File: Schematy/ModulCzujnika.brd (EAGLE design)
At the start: 22.8 x 44.1 mm, 10 parts, among them X1 GLX-S-88M

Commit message: Dodanie podciągającego rezystora na wyjście lm393
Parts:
- added R1: 10k, rcl:0207/7
- R12: value 100k -> 10k
- R13: value 1k -> 5k
- R14: value 1k -> 10k
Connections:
- net N$24: now also R1.2
- net VCC: now also R1.1
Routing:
- net N$24: track 22.5 -> 26.8 mm
- net VCC: track 42.9 -> 47.0 mm
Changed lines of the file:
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@@
 <attribute name="VALUE" x="0.1016" y="27.0256" size="1.27" layer="27" ratio="10" rot="R270"/>
 </element>
-<element name="R12" library="pot" library_urn="urn:adsk.eagle:library:331" package="CA6V" package3d_urn="urn:adsk.eagle:package:22691/1" value="100k" x="13.97" y="7.62" smashed="yes" rot="R90">
-<attribute name="NAME" x="9.779" y="5.08" size="1.27" layer="25" ratio="10" rot="R90"/>
+<element name="R12" library="pot" library_urn="urn:adsk.eagle:library:331" package="CA6V" package3d_urn="urn:adsk.eagle:package:22691/1" value="10k" x="13.97" y="7.62" smashed="yes" rot="R90">
+<attribute name="NAME" x="13.589" y="11.049" size="1.27" layer="25" ratio="10" rot="R180"/>
 <attribute name="POPULARITY" value="10" x="36.83" y="25.4" size="1.778" layer="27" rot="R90" display="off"/>
-<attribute name="VALUE" x="19.431" y="3.81" size="1.27" layer="27" ratio="10" rot="R90"/>
+<attribute name="VALUE" x="19.431" y="6.35" size="1.27" layer="27" ratio="10" rot="R90"/>
 </element>
-<element name="R13" library="rcl" library_urn="urn:adsk.eagle:library:334" package="0207/7" package3d_urn="urn:adsk.eagle:package:23493/2" value="1k" x="20.32" y="13.97" smashed="yes" rot="R90">
+<element name="R13" library="rcl" library_urn="urn:adsk.eagle:library:334" package="0207/7" package3d_urn="urn:adsk.eagle:package:23493/2" value="5k" x="20.32" y="13.97" smashed="yes" rot="R90">
 <attribute name="NAME" x="22.733" y="11.43" size="1.27" layer="25" ratio="10" rot="R90"/>
 <attribute name="POPULARITY" value="46" x="58.42" y="38.1" size="1.778" layer="27" rot="R90" display="off"/>
@@
 <attribute name="VALUE" x="20.8788" y="11.684" size="1.27" layer="27" ratio="10" rot="R90"/>
 </element>
-<element name="R14" library="rcl" library_urn="urn:adsk.eagle:library:334" package="0207/7" package3d_urn="urn:adsk.eagle:package:23493/2" value="1k" x="6.35" y="25.4" smashed="yes">
+<element name="R14" library="rcl" library_urn="urn:adsk.eagle:library:334" package="0207/7" package3d_urn="urn:adsk.eagle:package:23493/2" value="10k" x="6.35" y="25.4" smashed="yes">
 <attribute name="NAME" x="3.81" y="26.797" size="1.27" layer="25" ratio="10"/>
 <attribute name="POPULARITY" value="46" x="40.64" y="-12.7" size="1.778" layer="27" display="off"/>
@@
 <element name="U$4" library="BezkonataktowyLicznikObrotów" package="TO-92" value="DRV5053-Q1" x="13.97" y="2.54" smashed="yes" rot="R180">
 <attribute name="NAME" x="16.51" y="5.08" size="1.27" layer="21" rot="R180"/>
-<attribute name="VALUE" x="11.684" y="4.191" size="1.27" layer="21" rot="R180"/>
+<attribute name="VALUE" x="15.494" y="1.651" size="1.27" layer="21" rot="R180"/>
 </element>
 <element name="U$6" library="BezkonataktowyLicznikObrotów" package="R-PDIP-T8" value="LM393P" x="13.97" y="17.78" smashed="yes">
@@
 <attribute name="POPULARITY" value="3" x="34.29" y="26.67" size="1.778" layer="27" display="off"/>
 <attribute name="VALUE" x="6.35" y="38.1" size="1.27" layer="27"/>
+</element>
+<element name="R1" library="rcl" library_urn="urn:adsk.eagle:library:334" package="0207/7" package3d_urn="urn:adsk.eagle:package:23493/2" value="10k" x="8.636" y="6.096" smashed="yes" rot="R90">
+<attribute name="NAME" x="7.366" y="4.191" size="1.27" layer="25" ratio="10" rot="R180"/>
+<attribute name="POPULARITY" value="46" x="8.636" y="6.096" size="1.778" layer="27" rot="R90" display="off"/>
+<attribute name="SPICEPREFIX" value="R" x="8.636" y="6.096" size="1.778" layer="27" rot="R90" display="off"/>
+<attribute name="VALUE" x="9.1948" y="3.81" size="1.27" layer="27" ratio="10" rot="R90"/>
 </element>
 </elements>
@@
 <wire x1="7.239" y1="33.909" x2="7.239" y2="28.321" width="1.016" layer="16"/>
 <wire x1="7.239" y1="28.321" x2="10.16" y2="25.4" width="1.016" layer="16"/>
+<contactref element="R1" pad="1"/>
+<wire x1="12.7" y1="2.54" x2="12.446" y2="2.286" width="0.6096" layer="1"/>
+<wire x1="12.446" y1="2.286" x2="8.636" y2="2.286" width="0.6096" layer="1"/>
 </signal>
 <signal name="N$25">
@@
 <wire x1="5.08" y1="7.62" x2="5.08" y2="8.509" width="0.6096" layer="1"/>
 <wire x1="5.08" y1="8.509" x2="10.16" y2="13.589" width="0.6096" layer="1"/>
+<contactref element="R1" pad="2"/>
+<wire x1="10.16" y1="13.589" x2="10.16" y2="11.43" width="0.6096" layer="1"/>
+<wire x1="10.16" y1="11.43" x2="8.636" y2="9.906" width="0.6096" layer="1"/>
 </signal>
 <signal name="N$11">

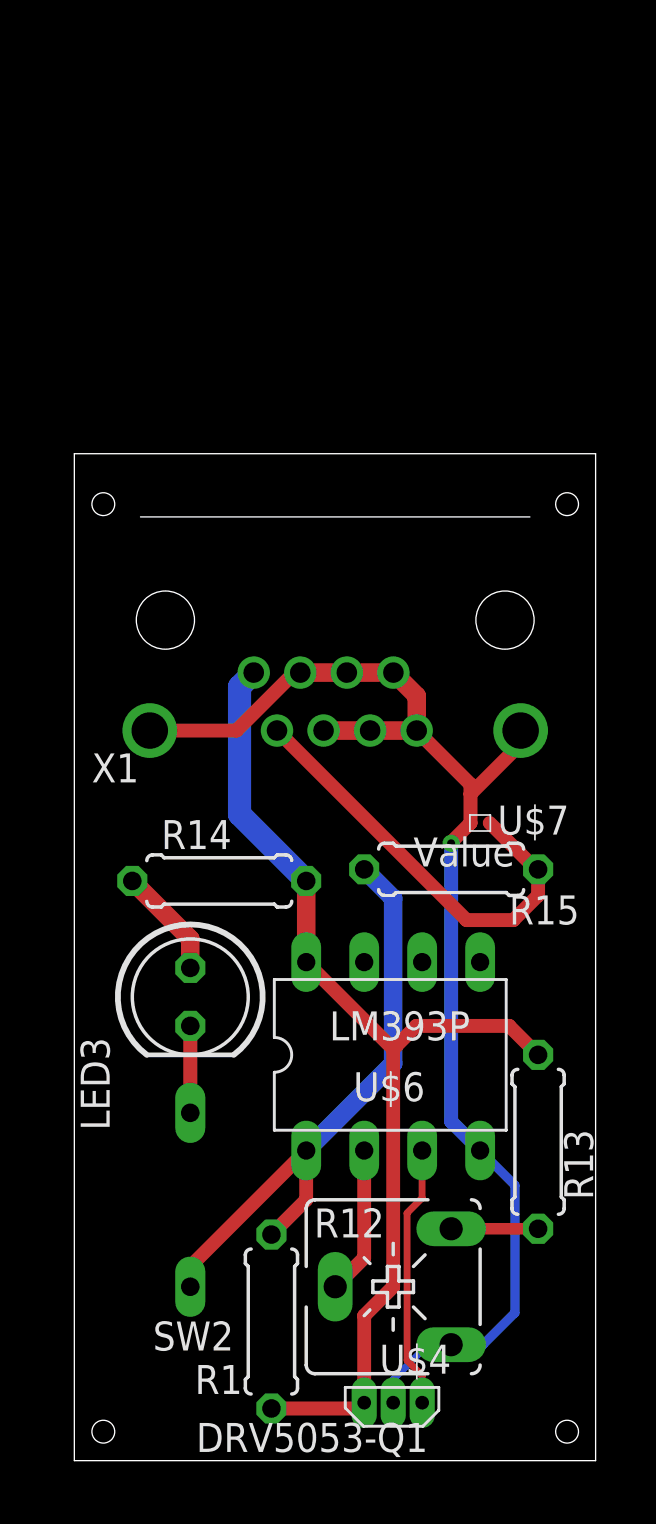
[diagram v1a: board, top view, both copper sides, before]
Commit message: Częściowe zabezpieczenie modułu czujnika
Częściowe zabezpieczenie modułu czujnika przed nagłym wzrostem napięcia na wejściu modułu.
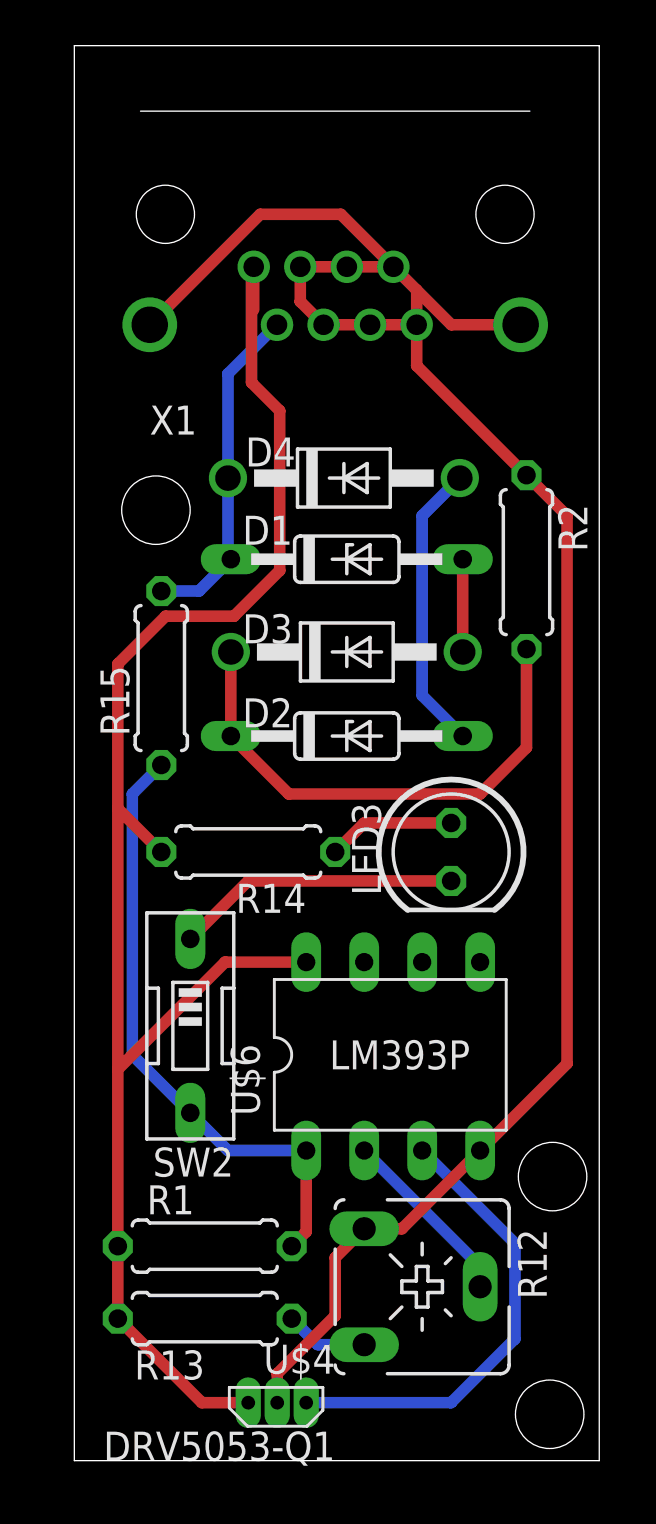
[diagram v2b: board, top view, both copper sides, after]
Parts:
- removed U$7: ESD9B3.3, BezkonataktowyLicznikObrotów:SOD-932
- added D1, D2: BZX55, diode:DO35Z10
- added D3, D4: 1N4004, diode:DO41-10
- added R2: 47, rcl:0207/7
- moved X1 17.8 mm to (11.4, 54.6)
- moved R13 16.5 mm to (5.71, 6.22), turned to 180 degrees
- moved R15 15.2 mm to (3.81, 34.3), turned to 90 degrees
- moved LED3 13.1 mm to (16.5, 26.7)
- moved SW2 7.62 mm to (5.08, 19.1), flipped to the top
- moved U$4 5.08 mm to (8.89, 2.54)
- moved R1 4.41 mm to (5.71, 9.40), turned to 0 degrees
- moved R14 1.80 mm to (7.62, 26.7), turned to 180 degrees
- moved R12 1.27 mm to (15.2, 7.62), turned to 270 degrees
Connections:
- new net N$1: D2.C, D3.C, R2.2
- new net N$3: D2.A, D4.A
- new net N$4: D1.A, D3.A
- net GND: now also R2.1; no longer U$7.1
- net N$2: now also D1.C, D4.C; no longer U$7.2
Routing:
- net GND: track 58.0 -> 89.1 mm, vias 1 -> 0
- net VCC: track 47.0 -> 73.4 mm
- net N$1: track 0.00 -> 22.8 mm
- net N$3: track 0.00 -> 12.7 mm
- net N$29: track 3.81 -> 12.5 mm
- net N$11: track 11.6 -> 20.2 mm
- net N$2: track 19.4 -> 14.8 mm
- net N$4: track 0.00 -> 4.06 mm
- net N$14: track 6.50 -> 8.07 mm
- net N$28: track 4.86 -> 5.61 mm
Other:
- board size 22.8 x 44.1 mm -> 23 x 62 mm
